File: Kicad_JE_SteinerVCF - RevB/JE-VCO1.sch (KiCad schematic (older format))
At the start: 56 parts, among them J301 Sine, J302 Tri, J303 Sq, J304 CV, J305 CV, P301 Doepfer_Power_10pin, U301 TL074, U302 ICL8038

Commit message: VCO minor
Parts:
- R328: value 0R -> 10R
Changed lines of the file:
@@
 P 7825 5600
 F 0 "R328" V 7618 5600 50  0000 C CNN
-F 1 "0R" V 7709 5600 50  0000 C CNN
+F 1 "10R" V 7709 5600 50  0000 C CNN
 F 2 "Resistor_SMD:R_0805_2012Metric_Pad1.15x1.40mm_HandSolder" V 7755 5600 50  0001 C CNN
 F 3 "~" H 7825 5600 50  0001 C CNN

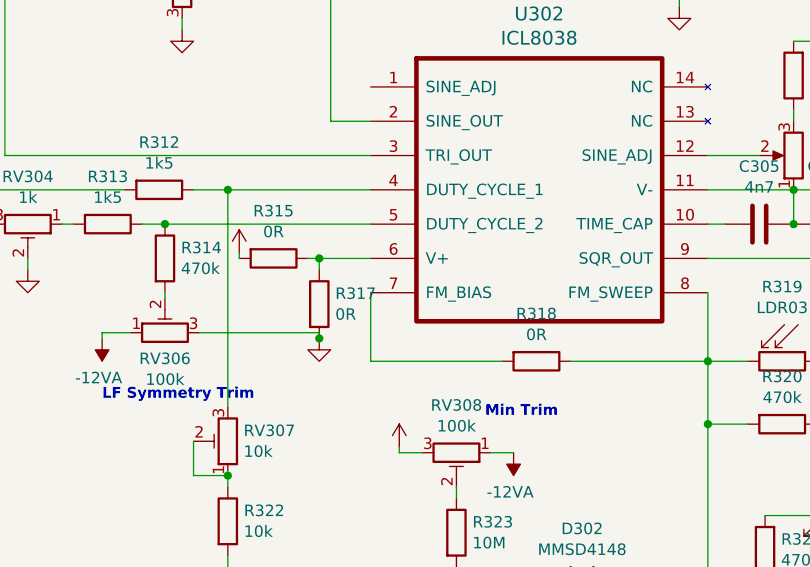
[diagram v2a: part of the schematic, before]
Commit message: VCO 0R indicate
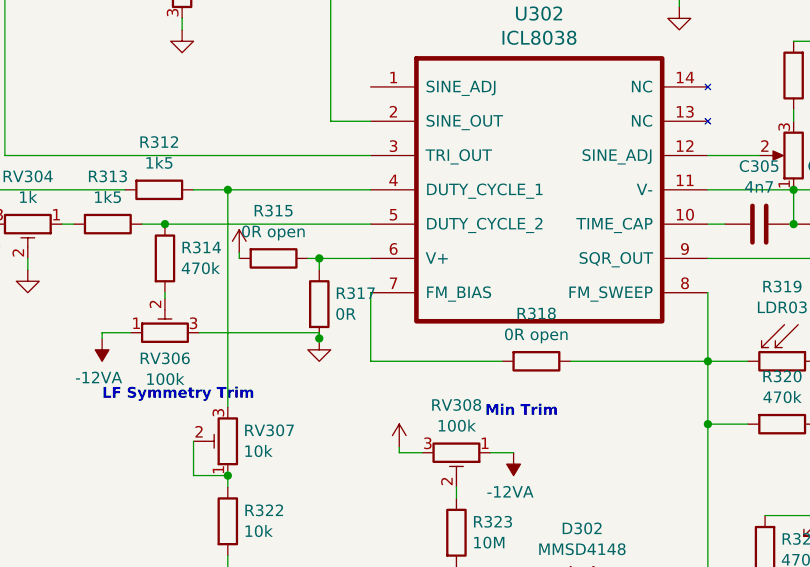
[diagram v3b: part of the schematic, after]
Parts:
- R315, R318: value 0R -> 0R open
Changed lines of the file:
@@
 P 6100 3450
 F 0 "R315" V 5893 3450 50  0000 C CNN
-F 1 "0R" V 5984 3450 50  0000 C CNN
+F 1 "0R open" V 5984 3450 50  0000 C CNN
 F 2 "Resistor_SMD:R_0805_2012Metric_Pad1.15x1.40mm_HandSolder" V 6030 3450 50  0001 C CNN
 F 3 "~" H 6100 3450 50  0001 C CNN
@@
 P 7250 3900
 F 0 "R318" V 7043 3900 50  0000 C CNN
-F 1 "0R" V 7134 3900 50  0000 C CNN
+F 1 "0R open" V 7134 3900 50  0000 C CNN
 F 2 "Resistor_SMD:R_0805_2012Metric_Pad1.15x1.40mm_HandSolder" V 7180 3900 50  0001 C CNN
 F 3 "~" H 7250 3900 50  0001 C CNN

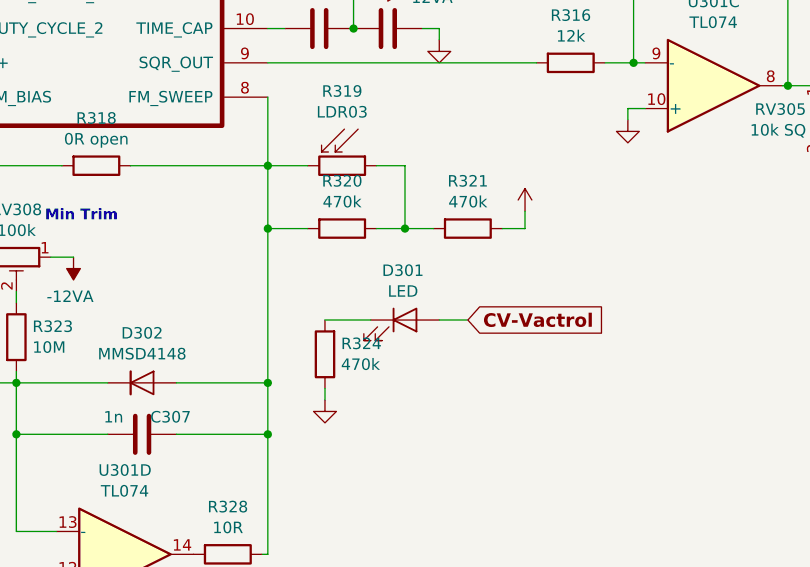
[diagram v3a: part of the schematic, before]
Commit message: vco updated values
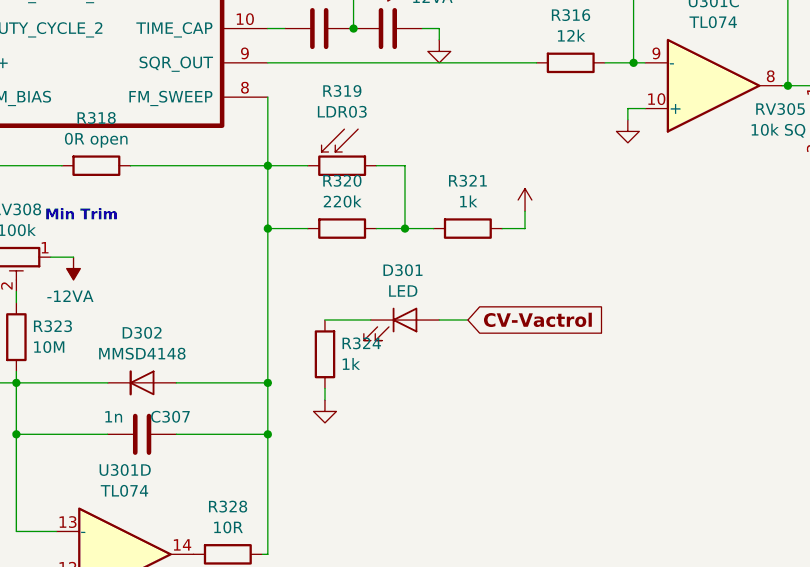
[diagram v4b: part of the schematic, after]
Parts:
- R320: value 470k -> 220k
- R321, R324: value 470k -> 1k
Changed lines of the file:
@@
 P 8325 4175
 F 0 "R320" V 8118 4175 50  0000 C CNN
-F 1 "470k" V 8209 4175 50  0000 C CNN
+F 1 "220k" V 8209 4175 50  0000 C CNN
 F 2 "Resistor_SMD:R_0805_2012Metric_Pad1.15x1.40mm_HandSolder" V 8255 4175 50  0001 C CNN
 F 3 "~" H 8325 4175 50  0001 C CNN
@@
 P 8875 4175
 F 0 "R321" V 8668 4175 50  0000 C CNN
-F 1 "470k" V 8759 4175 50  0000 C CNN
+F 1 "1k" V 8759 4175 50  0000 C CNN
 F 2 "Resistor_SMD:R_0805_2012Metric_Pad1.15x1.40mm_HandSolder" V 8805 4175 50  0001 C CNN
 F 3 "~" H 8875 4175 50  0001 C CNN
@@
 P 8250 4725
 F 0 "R324" H 8180 4679 50  0000 R CNN
-F 1 "470k" H 8180 4770 50  0000 R CNN
+F 1 "1k" H 8180 4770 50  0000 R CNN
 F 2 "Resistor_SMD:R_0805_2012Metric_Pad1.15x1.40mm_HandSolder" V 8180 4725 50  0001 C CNN
 F 3 "~" H 8250 4725 50  0001 C CNN

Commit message: RevB Sch initiated
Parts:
- removed D301: LED, LED_THT:LED_D5.0mm, symbol Device:LED
- removed R315, R318: 0R open, Resistor_SMD:R_0805_2012Metric_Pad1.15x1.40mm_HandSolder, symbol Device:R
- removed R317: 0R, Resistor_SMD:R_0805_2012Metric_Pad1.15x1.40mm_HandSolder, symbol Device:R
- removed R319: LDR03, OptoDevice:R_LDR_7x6mm_P5.1mm_Vertical, symbol Sensor_Optical:LDR03
- removed R321, R324: 1k, Resistor_SMD:R_0805_2012Metric_Pad1.15x1.40mm_HandSolder, symbol Device:R
- R307, R308: value 0R -> 680R
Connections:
- net +12VA: now also R320.1
- net GNDA: now also U302.6 (V+); no longer J301.TN, J302.TN, J303.TN
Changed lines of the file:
@@
 	1200 2900 1050 2900
-Wire Wire Line
-	1200 2900 1200 2650
 Wire Wire Line
 	1200 2450 1050 2450
 Connection ~ 1200 2900
 Wire Wire Line
-	1200 2450 1200 2250
-Wire Wire Line
 	1200 2050 1050 2050
 Connection ~ 1200 2450
-Wire Wire Line
-	1050 2250 1200 2250
-Connection ~ 1200 2250
-Wire Wire Line
-	1200 2250 1200 2050
-Wire Wire Line
-	1050 2650 1200 2650
-Connection ~ 1200 2650
-Wire Wire Line
-	1200 2650 1200 2450
-Wire Wire Line
-	1050 3100 1200 3100
-Wire Wire Line
-	1200 2900 1200 3100
 Text GLabel 1400 3000 2    59   Input ~ 12
 Square
@@
 Wire Wire Line
 	1050 3800 1200 3800
-Wire Wire Line
-	1050 4000 1200 4000
-Wire Wire Line
-	1200 3800 1200 4000
-Connection ~ 1200 4000
-Wire Wire Line
-	1200 4000 1200 4250
 Text GLabel 1400 3900 2    59   Input ~ 12
 CV-VCO
@@
 Wire Wire Line
 	2250 900  2500 900
-$Comp
-L Device:R R317
-U 1 1 5C6293BD
-P 6300 3650
-F 0 "R317" H 6370 3696 50  0000 L CNN
-F 1 "0R" H 6370 3605 50  0000 L CNN
-F 2 "Resistor_SMD:R_0805_2012Metric_Pad1.15x1.40mm_HandSolder" V 6230 3650 50  0001 C CNN
-F 3 "~" H 6300 3650 50  0001 C CNN
-	1    6300 3650
-	1    0    0    -1
-$EndComp
-$Comp
-L Device:R R315
-U 1 1 5C629478
-P 6100 3450
-F 0 "R315" V 5893 3450 50  0000 C CNN
-F 1 "0R open" V 5984 3450 50  0000 C CNN
-F 2 "Resistor_SMD:R_0805_2012Metric_Pad1.15x1.40mm_HandSolder" V 6030 3450 50  0001 C CNN
-F 3 "~" H 6100 3450 50  0001 C CNN
-	1    6100 3450
-	0    1    1    0
-$EndComp
 Wire Wire Line
 	6525 3450 6300 3450
-Wire Wire Line
-	6300 3500 6300 3450
 $Comp
 L power:GNDA #PWR?
@@
 F 3 "" H 6300 3800 50  0001 C CNN
 	1    6300 3800
-	1    0    0    -1
-$EndComp
-$Comp
-L power:+12VA #PWR?
-U 1 1 5C62B06C
-P 5950 3425
-AR Path="/5C62B06C" Ref="#PWR?"  Part="1"
-AR Path="/5C618010/5C62B06C" Ref="#PWR0315"  Part="1"
-F 0 "#PWR0315" H 5950 3275 50  0001 C CNN
-F 1 "+12VA" H 5965 3598 50  0001 C CNN
-F 2 "" H 5950 3425 50  0001 C CNN
-F 3 "" H 5950 3425 50  0001 C CNN
-	1    5950 3425
 	1    0    0    -1
 $EndComp
@@
 Wire Wire Line
 	8750 3300 8675 3300
-$Comp
-L Device:R R318
-U 1 1 5C632E13
-P 7250 3900
-F 0 "R318" V 7043 3900 50  0000 C CNN
-F 1 "0R open" V 7134 3900 50  0000 C CNN
-F 2 "Resistor_SMD:R_0805_2012Metric_Pad1.15x1.40mm_HandSolder" V 7180 3900 50  0001 C CNN
-F 3 "~" H 7250 3900 50  0001 C CNN
-	1    7250 3900
-	0    1    1    0
-$EndComp
-Wire Wire Line
-	6525 3600 6525 3900
-Wire Wire Line
-	6525 3900 7100 3900
-Wire Wire Line
-	7400 3900 8000 3900
-Wire Wire Line
-	8000 3900 8000 3600
 $Comp
 L Device:R R304
@@
 Wire Wire Line
 	5775 3775 6300 3775
-Wire Wire Line
-	6300 3775 6300 3800
-Connection ~ 6300 3800
 $Comp
 L power:-12VA #PWR?
@@
 	5900 3150 5900 4100
 Wire Wire Line
-	5950 3450 5950 3425
-Wire Wire Line
-	6250 3450 6300 3450
-Connection ~ 6300 3450
-Wire Wire Line
 	5750 4250 5750 4400
 Wire Wire Line
@@
 P 7875 1825
 F 0 "R307" H 7945 1871 50  0000 L CNN
-F 1 "0R" H 7945 1780 50  0000 L CNN
+F 1 "680R" H 7945 1780 50  0000 L CNN
 F 2 "Resistor_SMD:R_0805_2012Metric_Pad1.15x1.40mm_HandSolder" V 7805 1825 50  0001 C CNN
 F 3 "~" H 7875 1825 50  0001 C CNN
@@
 P 5700 1925
 F 0 "R308" H 5770 1971 50  0000 L CNN
-F 1 "0R" H 5770 1880 50  0000 L CNN
+F 1 "680R" H 5770 1880 50  0000 L CNN
 F 2 "Resistor_SMD:R_0805_2012Metric_Pad1.15x1.40mm_HandSolder" V 5630 1925 50  0001 C CNN
 F 3 "~" H 5700 1925 50  0001 C CNN
@@
 	0    1    1    0
 $EndComp
-Wire Wire Line
-	8000 3900 8000 4175
-Connection ~ 8000 3900
 Wire Wire Line
 	6900 4850 6900 5075
@@
 	8000 4850 8000 5075
 $Comp
-L Sensor_Optical:LDR03 R319
-U 1 1 5C777D17
-P 8325 3900
-F 0 "R319" V 8000 3900 50  0000 C CNN
-F 1 "LDR03" V 8091 3900 50  0000 C CNN
-F 2 "OptoDevice:R_LDR_7x6mm_P5.1mm_Vertical" V 8500 3900 50  0001 C CNN
-F 3 "http://www.elektronica-componenten.nl/WebRoot/StoreNL/Shops/61422969/54F1/BA0C/C664/31B9/2173/C0A8/2AB9/2AEF/LDR03IMP.pdf" H 8325 3850 50  0001 C CNN
-	1    8325 3900
-	0    1    1    0
-$EndComp
-$Comp
 L Device:R R320
 U 1 1 5C777F8D
@@
 $EndComp
 Wire Wire Line
-	8000 3900 8175 3900
-Wire Wire Line
 	8000 4175 8175 4175
 Connection ~ 8000 4175
 Wire Wire Line
 	8000 4175 8000 4850
-Wire Wire Line
-	8475 4175 8600 4175
-Wire Wire Line
-	8600 4175 8600 3900
-Wire Wire Line
-	8600 3900 8475 3900
-$Comp
-L Device:R R321
-U 1 1 5C78E5CC
-P 8875 4175
-F 0 "R321" V 8668 4175 50  0000 C CNN
-F 1 "1k" V 8759 4175 50  0000 C CNN
-F 2 "Resistor_SMD:R_0805_2012Metric_Pad1.15x1.40mm_HandSolder" V 8805 4175 50  0001 C CNN
-F 3 "~" H 8875 4175 50  0001 C CNN
-	1    8875 4175
-	0    1    1    0
-$EndComp
-Wire Wire Line
-	8600 4175 8725 4175
-Connection ~ 8600 4175
 $Comp
 L power:+12VA #PWR?
 U 1 1 5C796260
-P 9125 4100
+P 8825 4100
 AR Path="/5C796260" Ref="#PWR?"  Part="1"
 AR Path="/5C618010/5C796260" Ref="#PWR0321"  Part="1"
-F 0 "#PWR0321" H 9125 3950 50  0001 C CNN
-F 1 "+12VA" H 9140 4273 50  0001 C CNN
-F 2 "" H 9125 4100 50  0001 C CNN
-F 3 "" H 9125 4100 50  0001 C CNN
-	1    9125 4100
-	1    0    0    -1
-$EndComp
-Wire Wire Line
-	9025 4175 9125 4175
-Wire Wire Line
-	9125 4175 9125 4100
+F 0 "#PWR0321" H 8825 3950 50  0001 C CNN
+F 1 "+12VA" H 8840 4273 50  0001 C CNN
+F 2 "" H 8825 4100 50  0001 C CNN
+F 3 "" H 8825 4100 50  0001 C CNN
+	1    8825 4100
+	1    0    0    -1
+$EndComp
+Wire Wire Line
+	8825 4175 8825 4100
 $Comp
 L Connector:AudioJack2_SwitchT J?
@@
 	1200 3800 1200 3525
 Connection ~ 1200 3800
-Connection ~ 1200 3100
 Wire Wire Line
 	1050 3525 1200 3525
@@
 Connection ~ 1200 3325
 Wire Wire Line
-	1200 3325 1200 3100
-Wire Wire Line
 	1050 3425 1425 3425
-Text GLabel 8875 4575 2    59   Input ~ 12
-CV-Vactrol
-$Comp
-L Device:R R324
-U 1 1 5C7CF710
-P 8250 4725
-F 0 "R324" H 8180 4679 50  0000 R CNN
-F 1 "1k" H 8180 4770 50  0000 R CNN
-F 2 "Resistor_SMD:R_0805_2012Metric_Pad1.15x1.40mm_HandSolder" V 8180 4725 50  0001 C CNN
-F 3 "~" H 8250 4725 50  0001 C CNN
-	1    8250 4725
-	-1   0    0    1
-$EndComp
-$Comp
-L power:GNDA #PWR?
-U 1 1 5C7CF98D
-P 8250 4925
-AR Path="/5C7CF98D" Ref="#PWR?"  Part="1"
-AR Path="/5C618010/5C7CF98D" Ref="#PWR0325"  Part="1"
-F 0 "#PWR0325" H 8250 4675 50  0001 C CNN
-F 1 "GNDA" H 8255 4752 50  0001 C CNN
-F 2 "" H 8250 4925 50  0001 C CNN
-F 3 "" H 8250 4925 50  0001 C CNN
-	1    8250 4925
-	1    0    0    -1
-$EndComp
-Wire Wire Line
-	8250 4925 8250 4875
-$Comp
-L Device:LED D301
-U 1 1 5C7D8543
-P 8600 4575
-F 0 "D301" H 8591 4791 50  0000 C CNN
-F 1 "LED" H 8591 4700 50  0000 C CNN
-F 2 "LED_THT:LED_D5.0mm" H 8600 4575 50  0001 C CNN
-F 3 "~" H 8600 4575 50  0001 C CNN
-	1    8600 4575
-	1    0    0    -1
-$EndComp
-Wire Wire Line
-	8250 4575 8450 4575
-Wire Wire Line
-	8750 4575 8875 4575
 $Comp
 L Device:R_POT RV303
@@
 	-1   0    0    1
 $EndComp
+Wire Wire Line
+	1200 4000 1200 4250
+Wire Wire Line
+	1200 3800 1200 4000
+Connection ~ 1200 4000
+Wire Wire Line
+	1050 4000 1200 4000
+Wire Wire Line
+	1200 2900 1200 3325
+Wire Wire Line
+	1200 2450 1200 2900
+Wire Wire Line
+	1200 2050 1200 2450
+Wire Wire Line
+	8475 4175 8825 4175
+Wire Wire Line
+	8000 3600 8000 4175
+Wire Wire Line
+	6300 3450 6300 3775
+Connection ~ 6300 3775
+Wire Wire Line
+	6300 3775 6300 3800
 $EndSCHEMATC

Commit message: RevB second step
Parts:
- removed J304: CV, AJ-Dropbox-Kicad:PJ301SM, symbol Connector:AudioJack2_SwitchT
- removed RV307: 10k, Potentiometer_THT:Potentiometer_Piher_PT-6-V_Vertical, symbol Device:R_POT_TRIM
- removed RV308: 100k, Potentiometer_THT:Potentiometer_Piher_PT-6-V_Vertical, symbol Device:R_POT_TRIM
- added C?: 1u, Capacitor_SMD:C_0805_2012Metric_Pad1.15x1.40mm_HandSolder, symbol Device:C
- added R?: 680R, Resistor_SMD:R_0805_2012Metric_Pad1.15x1.40mm_HandSolder, symbol Device:R
- added R?: 100r, Resistor_SMD:R_0805_2012Metric_Pad1.15x1.40mm_HandSolder, symbol Device:R
- added RV?: 100k Glide, Potentiometer_THT:Potentiometer_Alps_RK09K_Single_Vertical, symbol Device:R_POT
- RV301: value 10k Sin -> 50k Sin
- RV302: value 10k Tri -> 50k Tri
- RV305: value 10k SQ -> 50k SQ
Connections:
- net -12VA: now also R323.2
- net GNDA: now also C?.1
- net at R312.1, U302.4 (DUTY_CYCLE_1): now also R322.1
- net at C307.2, D302.1 (K), R322.2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: now also R323.1; no longer R323.2
- net at R311.1, U301.8: now also R?.2; no longer RV305.1
- net at R325.2, RV309.2: now also RV?.1, RV?.2
- new net: R?.1, RV305.1
- new net: R?.1, RV?.3
- new net: C?.2, R?.2
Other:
- note added: "Max Trim"
- moved on the sheet: R309, R310, R311, R316, R323, RV303, RV305, RV309, U301C

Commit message: DRC RevB
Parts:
- gave numbers to parts that had none: 4
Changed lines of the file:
@@
 EESchema Schematic File Version 4
 LIBS:Kicad_JE_SteinerVCF-cache
-EELAYER 26 0
+EELAYER 29 0
 EELAYER END
 $Descr A4 11693 8268
@@
 Connection ~ 10175 3550
 $Comp
-L Device:R R?
+L Device:R R315
 U 1 1 5C928572
 P 10375 3550
-F 0 "R?" V 10275 3750 50  0000 L CNN
+F 0 "R315" V 10275 3750 50  0000 L CNN
 F 1 "680R" V 10275 3475 50  0000 L CNN
 F 2 "Resistor_SMD:R_0805_2012Metric_Pad1.15x1.40mm_HandSolder" V 10305 3550 50  0001 C CNN
@@
 	3225 4850 3775 4850
 $Comp
-L Device:R_POT RV?
+L Device:R_POT RV307
 U 1 1 5C9D37FF
 P 3775 5100
-F 0 "RV?" H 3705 5146 50  0000 R CNN
+F 0 "RV307" H 3705 5146 50  0000 R CNN
 F 1 "100k Glide" H 3705 5055 50  0000 R CNN
 F 2 "Potentiometer_THT:Potentiometer_Alps_RK09K_Single_Vertical" H 3775 5100 50  0001 C CNN
@@
 P 3775 5800
 AR Path="/5C9E1425" Ref="C?"  Part="1"
-AR Path="/5C618010/5C9E1425" Ref="C?"  Part="1"
-F 0 "C?" H 4025 5925 50  0000 C CNN
+AR Path="/5C618010/5C9E1425" Ref="C308"  Part="1"
+F 0 "C308" H 4025 5925 50  0000 C CNN
 F 1 "1u" H 4025 5800 50  0000 C CNN
 F 2 "Capacitor_SMD:C_0805_2012Metric_Pad1.15x1.40mm_HandSolder" H 3813 5650 50  0001 C CNN
@@
 P 3775 6025
 AR Path="/5C9E8849" Ref="#PWR?"  Part="1"
-AR Path="/5C618010/5C9E8849" Ref="#PWR?"  Part="1"
-F 0 "#PWR?" H 3775 5775 50  0001 C CNN
+AR Path="/5C618010/5C9E8849" Ref="#PWR0315"  Part="1"
+F 0 "#PWR0315" H 3775 5775 50  0001 C CNN
 F 1 "GNDA" H 3780 5852 50  0001 C CNN
 F 2 "" H 3775 6025 50  0001 C CNN
@@
 	3775 6025 3775 5950
 $Comp
-L Device:R R?
+L Device:R R317
 U 1 1 5C9F73A5
 P 3775 5500
-F 0 "R?" H 3845 5546 50  0000 L CNN
+F 0 "R317" H 3845 5546 50  0000 L CNN
 F 1 "100r" H 3845 5455 50  0000 L CNN
 F 2 "Resistor_SMD:R_0805_2012Metric_Pad1.15x1.40mm_HandSolder" V 3705 5500 50  0001 C CNN
